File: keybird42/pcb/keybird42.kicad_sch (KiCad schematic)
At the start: 173 parts, among them SW111 SW_MX, SW112 SW_MX, SW113 SW_MX, SW114 SW_MX, SW115 SW_MX, SW116 SW_MX, SW117 SW_MX, SW121 SW_MX, SW122 SW_MX, SW123 SW_MX, SW124 SW_MX, SW125 SW_MX, SW126 SW_MX, SW127 SW_MX, SW131 SW_MX, SW132 SW_MX, SW133 SW_MX, SW134 SW_MX, SW135 SW_MX, SW136 SW_MX, SW137 SW_MX, SW211 SW_MX, SW212 SW_MX, SW213 SW_MX, SW214 SW_MX, SW215 SW_MX, SW216 SW_MX, SW217 SW_MX, SW221 SW_MX, SW222 SW_MX, SW223 SW_MX, SW225 SW_MX, SW226 SW_MX, SW227 SW_MX, SW231 SW_MX, SW232 SW_MX, SW233 SW_MX, SW234 SW_MX, SW235 SW_MX, SW236 SW_MX, SW237 SW_MX, SW311 SW_MX, SW312 SW_MX, SW314 SW_MX, SW315 SW_MX, SW316 SW_MX, SW317 SW_MX, SW321 SW_MX, SW322 SW_MX, SW323 SW_MX, SW324 SW_MX, SW325 SW_MX, SW327 SW_MX, SW331 SW_MX, SW332 SW_MX, SW333 SW_MX, SW334 SW_MX, SW335 SW_MX, SW336 SW_MX, SW337 SW_MX, SW411 SW_MX, SW412 SW_MX, SW413 SW_MX, SW414 SW_MX, SW415 SW_MX, SW416 SW_MX, SW417 SW_MX, SW421 SW_MX, SW423 SW_MX, SW424 SW_MX, SW425 SW_MX, SW426 SW_MX, SW427 SW_MX, SW431 SW_MX, SW432 SW_MX, SW433 SW_MX, SW434 SW_MX, SW436 SW_MX, SW437 SW_MX, SW501 SW_MX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

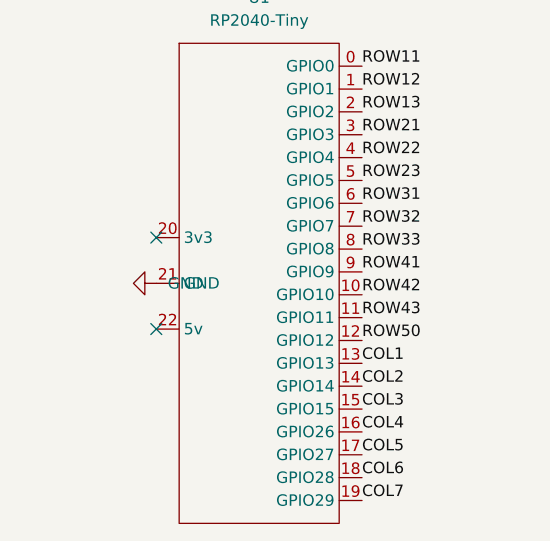
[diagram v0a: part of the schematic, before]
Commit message: move diodes to back and flip them
done by editing the libraries
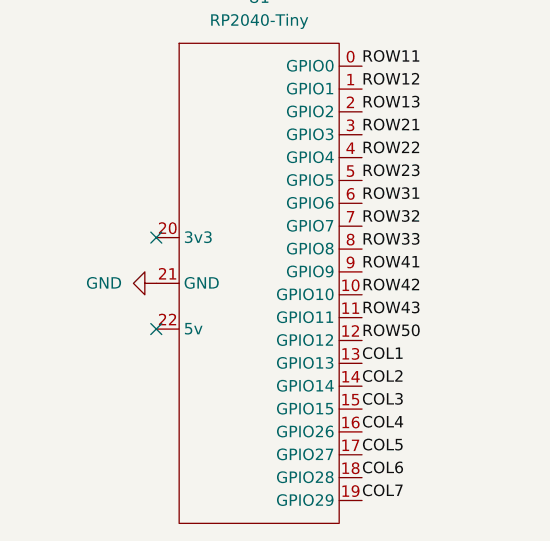
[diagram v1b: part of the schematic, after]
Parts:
- D111, D112, D113, D114, D115, D116, D117, D121, D122, D123, D124, D125, D126, D127, D131, D132, D133, D134, D135, D136, D137, D211, D212, D213, D214, D215, D216, D217, D221, D222, D223, D225, D226, D227, D231, D232, D233, D234, D235, D236, D237, D311, D312, D314, D315, D316, D317, D321, D322, D323, D324, D325, D327, D331, D332, D333, D334, D335, D336, D337, D411, D412, D413, D414, D415, D416, D417, D421, D423, D424, D425, D426, D427, D431, D432, D433, D434, D436, D437, D501, D502, D503, D504, D505, D506, D507: footprint Diode_SMD:D_SOD-123 -> keybird42:D_1206_HandSolder_Back

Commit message: add a footprint for the RP2040-Tiny
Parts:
- U1: footprint (none) -> keybird42:RP2040-Tiny
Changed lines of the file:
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@@
       (effects (font (size 1.27 1.27)))
     )
-    (property "Footprint" "" (at 44.45 241.3 0)
+    (property "Footprint" "keybird42:RP2040-Tiny" (at 44.45 210.82 0)
       (effects (font (size 1.27 1.27)) hide)
     )

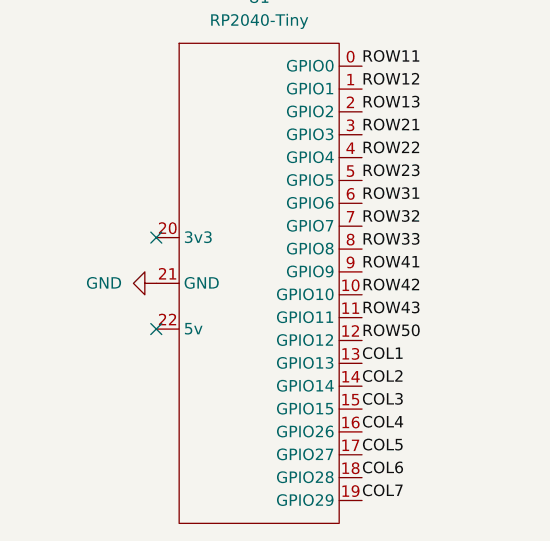
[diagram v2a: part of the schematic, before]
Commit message: diode reorg
swap pins of switches so diodes are wired to upper pads of sockets

change diodes to sod-123 because that's the commonly available kind

need to redo traces and vias
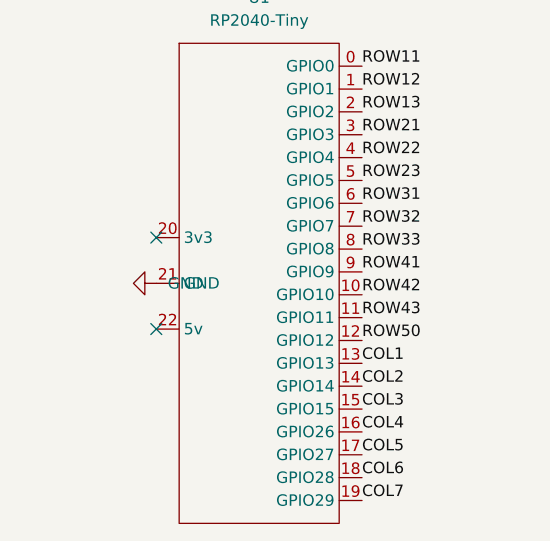
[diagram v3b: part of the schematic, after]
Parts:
- D111, D112, D113, D114, D115, D116, D117, D121, D122, D123, D124, D125, D126, D127, D131, D132, D133, D134, D135, D136, D137, D211, D212, D213, D214, D215, D216, D217, D221, D222, D223, D225, D226, D227, D231, D232, D233, D234, D235, D236, D237, D311, D312, D314, D315, D316, D317, D321, D322, D323, D324, D325, D327, D331, D332, D333, D334, D335, D336, D337, D411, D412, D413, D414, D415, D416, D417, D421, D423, D424, D425, D426, D427, D431, D432, D433, D434, D436, D437, D501, D502, D503, D504, D505, D506, D507: footprint keybird42:D_1206_HandSolder_Back -> keybird42:D_SOD-123_HandSolder_Back
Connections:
- net COL1: now also SW111.1, SW121.1, SW131.1, SW211.1, SW221.1, SW231.1, SW311.1, SW321.1, SW331.1, SW411.1, SW421.1, SW431.1, SW501.1; no longer SW111.2, SW121.2, SW131.2, SW211.2, SW221.2, SW231.2, SW311.2, SW321.2, SW331.2, SW411.2, SW421.2, SW431.2, SW501.2
- net COL2: now also SW112.1, SW122.1, SW132.1, SW212.1, SW222.1, SW232.1, SW312.1, SW322.1, SW332.1, SW412.1, SW432.1, SW502.1; no longer SW112.2, SW122.2, SW132.2, SW212.2, SW222.2, SW232.2, SW312.2, SW322.2, SW332.2, SW412.2, SW432.2, SW502.2
- net COL3: now also SW113.1, SW123.1, SW133.1, SW213.1, SW223.1, SW233.1, SW323.1, SW333.1, SW413.1, SW423.1, SW433.1, SW503.1; no longer SW113.2, SW123.2, SW133.2, SW213.2, SW223.2, SW233.2, SW323.2, SW333.2, SW413.2, SW423.2, SW433.2, SW503.2
- net COL4: now also SW114.1, SW124.1, SW134.1, SW214.1, SW234.1, SW314.1, SW324.1, SW334.1, SW414.1, SW424.1, SW434.1, SW504.1; no longer SW114.2, SW124.2, SW134.2, SW214.2, SW234.2, SW314.2, SW324.2, SW334.2, SW414.2, SW424.2, SW434.2, SW504.2
- net COL5: now also SW115.1, SW125.1, SW135.1, SW215.1, SW225.1, SW235.1, SW315.1, SW325.1, SW335.1, SW415.1, SW425.1, SW505.1; no longer SW115.2, SW125.2, SW135.2, SW215.2, SW225.2, SW235.2, SW315.2, SW325.2, SW335.2, SW415.2, SW425.2, SW505.2
- net COL6: now also SW116.1, SW126.1, SW136.1, SW216.1, SW226.1, SW236.1, SW316.1, SW336.1, SW416.1, SW426.1, SW436.1, SW506.1; no longer SW116.2, SW126.2, SW136.2, SW216.2, SW226.2, SW236.2, SW316.2, SW336.2, SW416.2, SW426.2, SW436.2, SW506.2
- net COL7: now also SW117.1, SW127.1, SW137.1, SW217.1, SW227.1, SW237.1, SW317.1, SW327.1, SW337.1, SW417.1, SW427.1, SW437.1, SW507.1; no longer SW117.2, SW127.2, SW137.2, SW217.2, SW227.2, SW237.2, SW317.2, SW327.2, SW337.2, SW417.2, SW427.2, SW437.2, SW507.2
- net at D327.2 (A): now also SW327.2; no longer SW327.1
- net at D423.2 (A): now also SW423.2; no longer SW423.1
- net at D436.2 (A): now also SW436.2; no longer SW436.1
- net at D214.2 (A): now also SW214.2; no longer SW214.1
- net at D505.2 (A): now also SW505.2; no longer SW505.1
- net at D416.2 (A): now also SW416.2; no longer SW416.1
- net at D115.2 (A): now also SW115.2; no longer SW115.1
- net at D417.2 (A): now also SW417.2; no longer SW417.1
- net at D215.2 (A): now also SW215.2; no longer SW215.1
- net at D431.2 (A): now also SW431.2; no longer SW431.1
- net at D227.2 (A): now also SW227.2; no longer SW227.1
- net at D427.2 (A): now also SW427.2; no longer SW427.1
- net at D211.2 (A): now also SW211.2; no longer SW211.1
- net at D412.2 (A): now also SW412.2; no longer SW412.1
- net at D503.2 (A): now also SW503.2; no longer SW503.1
- net at D135.2 (A): now also SW135.2; no longer SW135.1
- net at D223.2 (A): now also SW223.2; no longer SW223.1
- net at D323.2 (A): now also SW323.2; no longer SW323.1
- net at D321.2 (A): now also SW321.2; no longer SW321.1
- net at D213.2 (A): now also SW213.2; no longer SW213.1
- net at D235.2 (A): now also SW235.2; no longer SW235.1
- net at D425.2 (A): now also SW425.2; no longer SW425.1
- net at D315.2 (A): now also SW315.2; no longer SW315.1
- net at D316.2 (A): now also SW316.2; no longer SW316.1
- net at D314.2 (A): now also SW314.2; no longer SW314.1
- net at D133.2 (A): now also SW133.2; no longer SW133.1
- net at D432.2 (A): now also SW432.2; no longer SW432.1
- net at D311.2 (A): now also SW311.2; no longer SW311.1
- net at D335.2 (A): now also SW335.2; no longer SW335.1
- net at D332.2 (A): now also SW332.2; no longer SW332.1
- net at D212.2 (A): now also SW212.2; no longer SW212.1
- net at D117.2 (A): now also SW117.2; no longer SW117.1
- net at D413.2 (A): now also SW413.2; no longer SW413.1
- net at D113.2 (A): now also SW113.2; no longer SW113.1
- net at D114.2 (A): now also SW114.2; no longer SW114.1
- net at D226.2 (A): now also SW226.2; no longer SW226.1
- net at D222.2 (A): now also SW222.2; no longer SW222.1
- net at D221.2 (A): now also SW221.2; no longer SW221.1
- net at D122.2 (A): now also SW122.2; no longer SW122.1
- net at D434.2 (A): now also SW434.2; no longer SW434.1
- net at D415.2 (A): now also SW415.2; no longer SW415.1
- net at D124.2 (A): now also SW124.2; no longer SW124.1
- net at D234.2 (A): now also SW234.2; no longer SW234.1
- net at D437.2 (A): now also SW437.2; no longer SW437.1
- net at D121.2 (A): now also SW121.2; no longer SW121.1
- net at D137.2 (A): now also SW137.2; no longer SW137.1
- net at D414.2 (A): now also SW414.2; no longer SW414.1
- net at D506.2 (A): now also SW506.2; no longer SW506.1
- net at D217.2 (A): now also SW217.2; no longer SW217.1
- net at D331.2 (A): now also SW331.2; no longer SW331.1
- net at D336.2 (A): now also SW336.2; no longer SW336.1
- net at D233.2 (A): now also SW233.2; no longer SW233.1
- net at D501.2 (A): now also SW501.2; no longer SW501.1
- net at D236.2 (A): now also SW236.2; no longer SW236.1
- net at D433.2 (A): now also SW433.2; no longer SW433.1
- net at D123.2 (A): now also SW123.2; no longer SW123.1
- net at D317.2 (A): now also SW317.2; no longer SW317.1
- net at D334.2 (A): now also SW334.2; no longer SW334.1
- net at D337.2 (A): now also SW337.2; no longer SW337.1
- net at D333.2 (A): now also SW333.2; no longer SW333.1
- net at D131.2 (A): now also SW131.2; no longer SW131.1
- net at D411.2 (A): now also SW411.2; no longer SW411.1
- net at D232.2 (A): now also SW232.2; no longer SW232.1
- net at D502.2 (A): now also SW502.2; no longer SW502.1
- net at D507.2 (A): now also SW507.2; no longer SW507.1
- net at D126.2 (A): now also SW126.2; no longer SW126.1
- net at D127.2 (A): now also SW127.2; no longer SW127.1
- net at D136.2 (A): now also SW136.2; no longer SW136.1
- net at D132.2 (A): now also SW132.2; no longer SW132.1
- net at D134.2 (A): now also SW134.2; no longer SW134.1
- net at D225.2 (A): now also SW225.2; no longer SW225.1
- net at D237.2 (A): now also SW237.2; no longer SW237.1
- net at D324.2 (A): now also SW324.2; no longer SW324.1
- net at D216.2 (A): now also SW216.2; no longer SW216.1
- net at D421.2 (A): now also SW421.2; no longer SW421.1
- net at D322.2 (A): now also SW322.2; no longer SW322.1
- net at D112.2 (A): now also SW112.2; no longer SW112.1
- net at D424.2 (A): now also SW424.2; no longer SW424.1
- net at D312.2 (A): now also SW312.2; no longer SW312.1
- net at D111.2 (A): now also SW111.2; no longer SW111.1
- net at D116.2 (A): now also SW116.2; no longer SW116.1
- net at D325.2 (A): now also SW325.2; no longer SW325.1
- net at D504.2 (A): now also SW504.2; no longer SW504.1
- net at D231.2 (A): now also SW231.2; no longer SW231.1
- net at D125.2 (A): now also SW125.2; no longer SW125.1
- net at D426.2 (A): now also SW426.2; no longer SW426.1

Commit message: reduce silkscreen clutter
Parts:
- SW111, SW112, SW113, SW114, SW115, SW116, SW117, SW121, SW122, SW123, SW124, SW125, SW126, SW127, SW131, SW132, SW133, SW134, SW135, SW136, SW137, SW211, SW212, SW213, SW214, SW215, SW216, SW217, SW221, SW222, SW223, SW225, SW226, SW227, SW231, SW232, SW233, SW234, SW235, SW236, SW237, SW311, SW312, SW314, SW315, SW316, SW317, SW321, SW322, SW323, SW324, SW325, SW327, SW331, SW332, SW333, SW334, SW335, SW336, SW337, SW411, SW412, SW413, SW414, SW415, SW416, SW417, SW421, SW423, SW424, SW425, SW426, SW427, SW431, SW432, SW433, SW434, SW436, SW437, SW501, SW502, SW503, SW504, SW505, SW506, SW507: footprint PCM_Switch_Keyboard_Hotswap_Kailh:SW_Hotswap_Kailh_MX -> keybird42:SW_Hotswap_Kailh_MX

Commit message: fix DRC errors
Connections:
- net COL1: now also U1.1 (GPIO1); no longer U1.13 (GPIO13)
- net COL2: now also U1.6 (GPIO6); no longer U1.14 (GPIO14)
- net COL3: now also U1.14 (GPIO14); no longer U1.15 (GPIO15)
- net COL4: now also U1.9 (GPIO9); no longer U1.16 (GPIO26)
- net COL5: now also U1.15 (GPIO15); no longer U1.17 (GPIO27)
- net COL6: now also U1.5 (GPIO5); no longer U1.18 (GPIO28)
- net COL7: now also U1.2 (GPIO2); no longer U1.19 (GPIO29)
- net ROW12: now also U1.3 (GPIO3); no longer U1.1 (GPIO1)
- net ROW13: now also U1.19 (GPIO29); no longer U1.2 (GPIO2)
- net ROW21: now also U1.17 (GPIO27); no longer U1.3 (GPIO3)
- net ROW23: now also U1.18 (GPIO28); no longer U1.5 (GPIO5)
- net ROW31: now also U1.16 (GPIO26); no longer U1.6 (GPIO6)
- net ROW41: now also U1.10 (GPIO10); no longer U1.9 (GPIO9)
- net ROW42: now also U1.11 (GPIO11); no longer U1.10 (GPIO10)
- net ROW43: now also U1.12 (GPIO12); no longer U1.11 (GPIO11)
- net ROW50: now also U1.13 (GPIO13); no longer U1.12 (GPIO12)
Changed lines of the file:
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@@
     (stroke (width 0) (type default))
   )
-  (label "ROW21" (at 55.88 224.79 0) (fields_autoplaced)
+  (label "ROW12" (at 55.88 224.79 0) (fields_autoplaced)
     (effects (font (size 1.27 1.27)) (justify left bottom))
   )
@@
     (effects (font (size 1.27 1.27)) (justify right bottom))
   )
-  (label "ROW43" (at 55.88 245.11 0) (fields_autoplaced)
+  (label "ROW42" (at 55.88 245.11 0) (fields_autoplaced)
     (effects (font (size 1.27 1.27)) (justify left bottom))
   )
@@
     (effects (font (size 1.27 1.27)) (justify right bottom))
   )
-  (label "ROW50" (at 55.88 247.65 0) (fields_autoplaced)
+  (label "ROW43" (at 55.88 247.65 0) (fields_autoplaced)
     (effects (font (size 1.27 1.27)) (justify left bottom))
   )
@@
     (effects (font (size 1.27 1.27)) (justify right bottom))
   )
-  (label "COL7" (at 55.88 265.43 0) (fields_autoplaced)
+  (label "ROW13" (at 55.88 265.43 0) (fields_autoplaced)
     (effects (font (size 1.27 1.27)) (justify left bottom))
   )
-  (label "ROW23" (at 55.88 229.87 0) (fields_autoplaced)
+  (label "COL6" (at 55.88 229.87 0) (fields_autoplaced)
     (effects (font (size 1.27 1.27)) (justify left bottom))
   )
@@
     (effects (font (size 1.27 1.27)) (justify right bottom))
   )
-  (label "COL6" (at 55.88 262.89 0) (fields_autoplaced)
+  (label "ROW23" (at 55.88 262.89 0) (fields_autoplaced)
     (effects (font (size 1.27 1.27)) (justify left bottom))
   )
-  (label "ROW31" (at 55.88 232.41 0) (fields_autoplaced)
+  (label "COL2" (at 55.88 232.41 0) (fields_autoplaced)
     (effects (font (size 1.27 1.27)) (justify left bottom))
   )
@@
     (effects (font (size 1.27 1.27)) (justify left bottom))
   )
-  (label "COL5" (at 55.88 260.35 0) (fields_autoplaced)
+  (label "ROW21" (at 55.88 260.35 0) (fields_autoplaced)
     (effects (font (size 1.27 1.27)) (justify left bottom))
   )
@@
     (effects (font (size 1.27 1.27)) (justify right bottom))
   )
-  (label "COL1" (at 55.88 250.19 0) (fields_autoplaced)
+  (label "ROW50" (at 55.88 250.19 0) (fields_autoplaced)
     (effects (font (size 1.27 1.27)) (justify left bottom))
   )
-  (label "ROW42" (at 55.88 242.57 0) (fields_autoplaced)
+  (label "ROW41" (at 55.88 242.57 0) (fields_autoplaced)
     (effects (font (size 1.27 1.27)) (justify left bottom))
   )
@@
     (effects (font (size 1.27 1.27)) (justify left bottom))
   )
-  (label "COL2" (at 55.88 252.73 0) (fields_autoplaced)
+  (label "COL3" (at 55.88 252.73 0) (fields_autoplaced)
     (effects (font (size 1.27 1.27)) (justify left bottom))
   )
-  (label "COL3" (at 55.88 255.27 0) (fields_autoplaced)
+  (label "COL5" (at 55.88 255.27 0) (fields_autoplaced)
     (effects (font (size 1.27 1.27)) (justify left bottom))
   )
-  (label "ROW41" (at 55.88 240.03 0) (fields_autoplaced)
+  (label "COL4" (at 55.88 240.03 0) (fields_autoplaced)
     (effects (font (size 1.27 1.27)) (justify left bottom))
   )
-  (label "ROW13" (at 55.88 222.25 0) (fields_autoplaced)
+  (label "COL7" (at 55.88 222.25 0) (fields_autoplaced)
     (effects (font (size 1.27 1.27)) (justify left bottom))
   )
@@
     (effects (font (size 1.27 1.27)) (justify right bottom))
   )
-  (label "ROW12" (at 55.88 219.71 0) (fields_autoplaced)
+  (label "COL1" (at 55.88 219.71 0) (fields_autoplaced)
     (effects (font (size 1.27 1.27)) (justify left bottom))
   )
@@
     (effects (font (size 1.27 1.27)) (justify right bottom))
   )
-  (label "COL4" (at 55.88 257.81 0) (fields_autoplaced)
+  (label "ROW31" (at 55.88 257.81 0) (fields_autoplaced)
     (effects (font (size 1.27 1.27)) (justify left bottom))
   )
